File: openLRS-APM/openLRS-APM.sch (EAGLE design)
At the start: 24 parts, among them IC1 MCP1703CB, IC2 RFM23BPSMD, J1 CON_HEADER_PRG_AVR_ICSP-SMD, Y1 16MHz

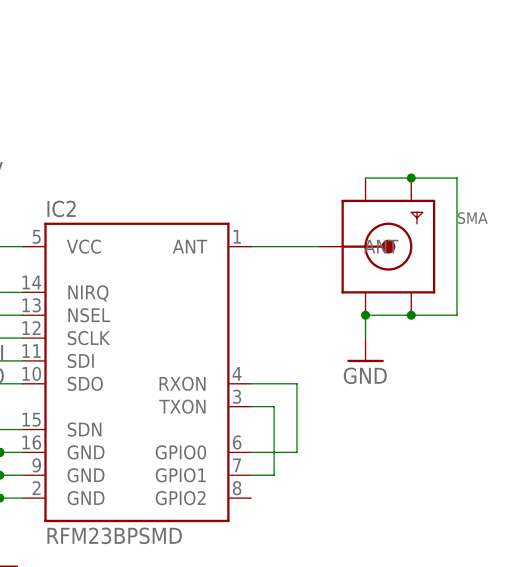
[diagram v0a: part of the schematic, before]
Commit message: Production Rev.1, changed the SMA connector.
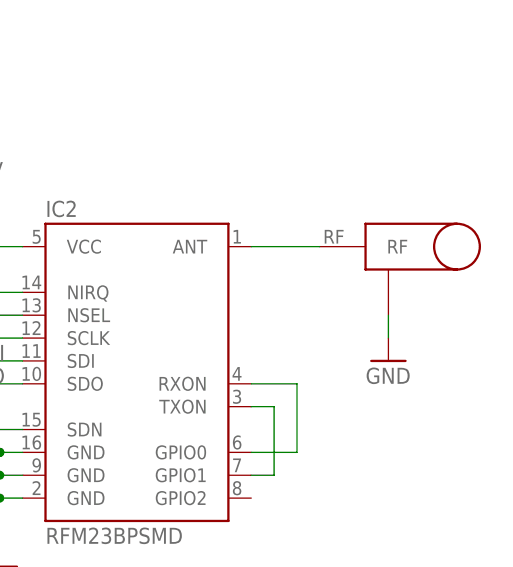
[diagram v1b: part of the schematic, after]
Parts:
- removed SMA: (no value), adafruit:SMACONNECTOR_EDGE
- added U$4: LINX-SMA, OpenLRS-APM:LINX-SMA
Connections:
- net GND: now also U$4.GND; no longer SMA.GND1, SMA.GND2, SMA.GND3, SMA.GND4
- net N$13: now also U$4.RF; no longer SMA.ANT
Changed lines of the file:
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@@
 <?xml version="1.0" encoding="utf-8"?>
 <!DOCTYPE eagle SYSTEM "eagle.dtd">
-<eagle version="7.1.0">
+<eagle version="7.2.0">
 <drawing>
 <settings>
@@
 <layer number="56" name="wert" color="7" fill="1" visible="no" active="no"/>
 <layer number="57" name="tCAD" color="7" fill="1" visible="no" active="no"/>
+<layer number="90" name="Modules" color="5" fill="1" visible="yes" active="yes"/>
 <layer number="91" name="Nets" color="2" fill="1" visible="yes" active="yes"/>
 <layer number="92" name="Busses" color="1" fill="1" visible="yes" active="yes"/>
@@
 <part name="C6" library="SparkFun-Capacitors" deviceset="CAP" device="0805" value="100n"/>
 <part name="GND7" library="SparkFun-Aesthetics" deviceset="GND" device=""/>
-<part name="SMA" library="adafruit" deviceset="SMACONNECTOR" device="_EDGE" value=" "/>
 <part name="IC1" library="linear" deviceset="MCP1703" device="CB"/>
 <part name="GND3" library="SparkFun-Aesthetics" deviceset="GND" device=""/>
@@
 <part name="GND8" library="SparkFun-Aesthetics" deviceset="GND" device=""/>
 <part name="J1" library="dp_devices" deviceset="CON_HEADER_PRG_AVR_ICSP" device="-SMD"/>
+<part name="U$4" library="OpenLRS-APM" deviceset="LINX-SMA" device=""/>
 </parts>
 <sheets>
@@
 <instance part="C4" gate="G$1" x="20.32" y="40.64" rot="R270"/>
 <instance part="GND5" gate="1" x="35.56" y="33.02"/>
-<instance part="GND6" gate="1" x="187.96" y="66.04"/>
+<instance part="GND6" gate="1" x="190.5" y="66.04"/>
 <instance part="Y1" gate="G$1" x="30.48" y="43.18" rot="R90"/>
 <instance part="C9" gate="G$1" x="132.08" y="81.28"/>
@@
 <instance part="C6" gate="G$1" x="30.48" y="78.74" rot="R90"/>
 <instance part="GND7" gate="1" x="25.4" y="73.66"/>
-<instance part="SMA" gate="G$1" x="190.5" y="78.74"/>
 <instance part="IC1" gate="G$1" x="60.96" y="119.38"/>
 <instance part="GND3" gate="1" x="60.96" y="109.22"/>
@@
 <instance part="GND8" gate="1" x="25.4" y="58.42"/>
 <instance part="J1" gate="J" x="-25.4" y="45.72"/>
+<instance part="U$4" gate="G$1" x="187.96" y="78.74"/>
 </instances>
 <busses>
@@
 </segment>
 <segment>
-<pinref part="GND6" gate="1" pin="GND"/>
-<wire x1="187.96" y1="71.12" x2="187.96" y2="68.58" width="0.1524" layer="91"/>
-<pinref part="SMA" gate="G$1" pin="GND4"/>
-<wire x1="187.96" y1="71.12" x2="193.04" y2="71.12" width="0.1524" layer="91"/>
-<wire x1="193.04" y1="71.12" x2="198.12" y2="71.12" width="0.1524" layer="91"/>
-<wire x1="198.12" y1="71.12" x2="198.12" y2="86.36" width="0.1524" layer="91"/>
-<pinref part="SMA" gate="G$1" pin="GND2"/>
-<wire x1="198.12" y1="86.36" x2="193.04" y2="86.36" width="0.1524" layer="91"/>
-<pinref part="SMA" gate="G$1" pin="GND1"/>
-<wire x1="193.04" y1="86.36" x2="187.96" y2="86.36" width="0.1524" layer="91"/>
-<junction x="193.04" y="71.12"/>
-<junction x="193.04" y="86.36"/>
-<pinref part="SMA" gate="G$1" pin="GND3"/>
-<junction x="187.96" y="71.12"/>
-</segment>
-<segment>
 <pinref part="C6" gate="G$1" pin="1"/>
 <pinref part="GND7" gate="1" pin="GND"/>
@@
 <label x="-12.7" y="43.18" size="1.778" layer="95"/>
 </segment>
+<segment>
+<pinref part="GND6" gate="1" pin="GND"/>
+<pinref part="U$4" gate="G$1" pin="GND"/>
+<wire x1="190.5" y1="68.58" x2="190.5" y2="71.12" width="0.1524" layer="91"/>
+</segment>
 </net>
 <net name="/RESET" class="0">
@@
 <pinref part="IC2" gate="G$1" pin="ANT"/>
 <wire x1="175.26" y1="78.74" x2="182.88" y2="78.74" width="0.1524" layer="91"/>
-<pinref part="SMA" gate="G$1" pin="ANT"/>
-</segment>
-</net>
+<pinref part="U$4" gate="G$1" pin="RF"/>
+</segment>
+</net>
